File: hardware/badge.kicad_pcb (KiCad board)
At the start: 2 copper layers, 88 x 156.6 mm, 125 parts, among them J1 Micro_SD_Card, J2 MY-18650-01, J3 Conn_01x40, J4 USB_C_Receptacle_USB2.0_14P, J5 MY-18650-01, Q1 AO3400A, Q3 AO3400A, SW1 SW_Push, SW10 SW_Push, SW11 SW_Push, SW12 SW_Push, SW13 SW_Push, SW14 SW_Push, SW15 SW_Push, SW16 SW_Push, SW17 SW_Push, SW18 SW_Push, SW19 SW_Push, SW2 SW_Push, SW20 SW_Push, SW21 SW_Push, SW22 SW_Push, SW23 SW_Push, SW25 SW_Push, SW26 SW_Push, SW27 SW_Push, SW28 SW_Push, SW29 SW_Push, SW3 SW_Push, SW30 SW_Push, SW31 SW_Push, SW33 SW_Push, SW34 SW_Push, SW35 SW_Push, SW36 SW_Push, SW37 SW_Push, SW38 SW_Push, SW39 SW_Push, SW4 SW_Push, SW5 SW_Push, SW57 MK-12C02-G020, SW58 SKRHABE010, SW6 SW_Push, SW7 SW_Push, SW8 BOOT, SW9 SW_Push, U1 ESP32-S3-WROOM-1, U10 PCA9555PW, U11 PCA9555PW, U3 BQ24075RGT, U4 TLV62569DBV, U5 BME280, U6 USBLC6-2P6, U7 BMI270, U8 Ai-Thinker-Ra-02, U9 MAX98357A

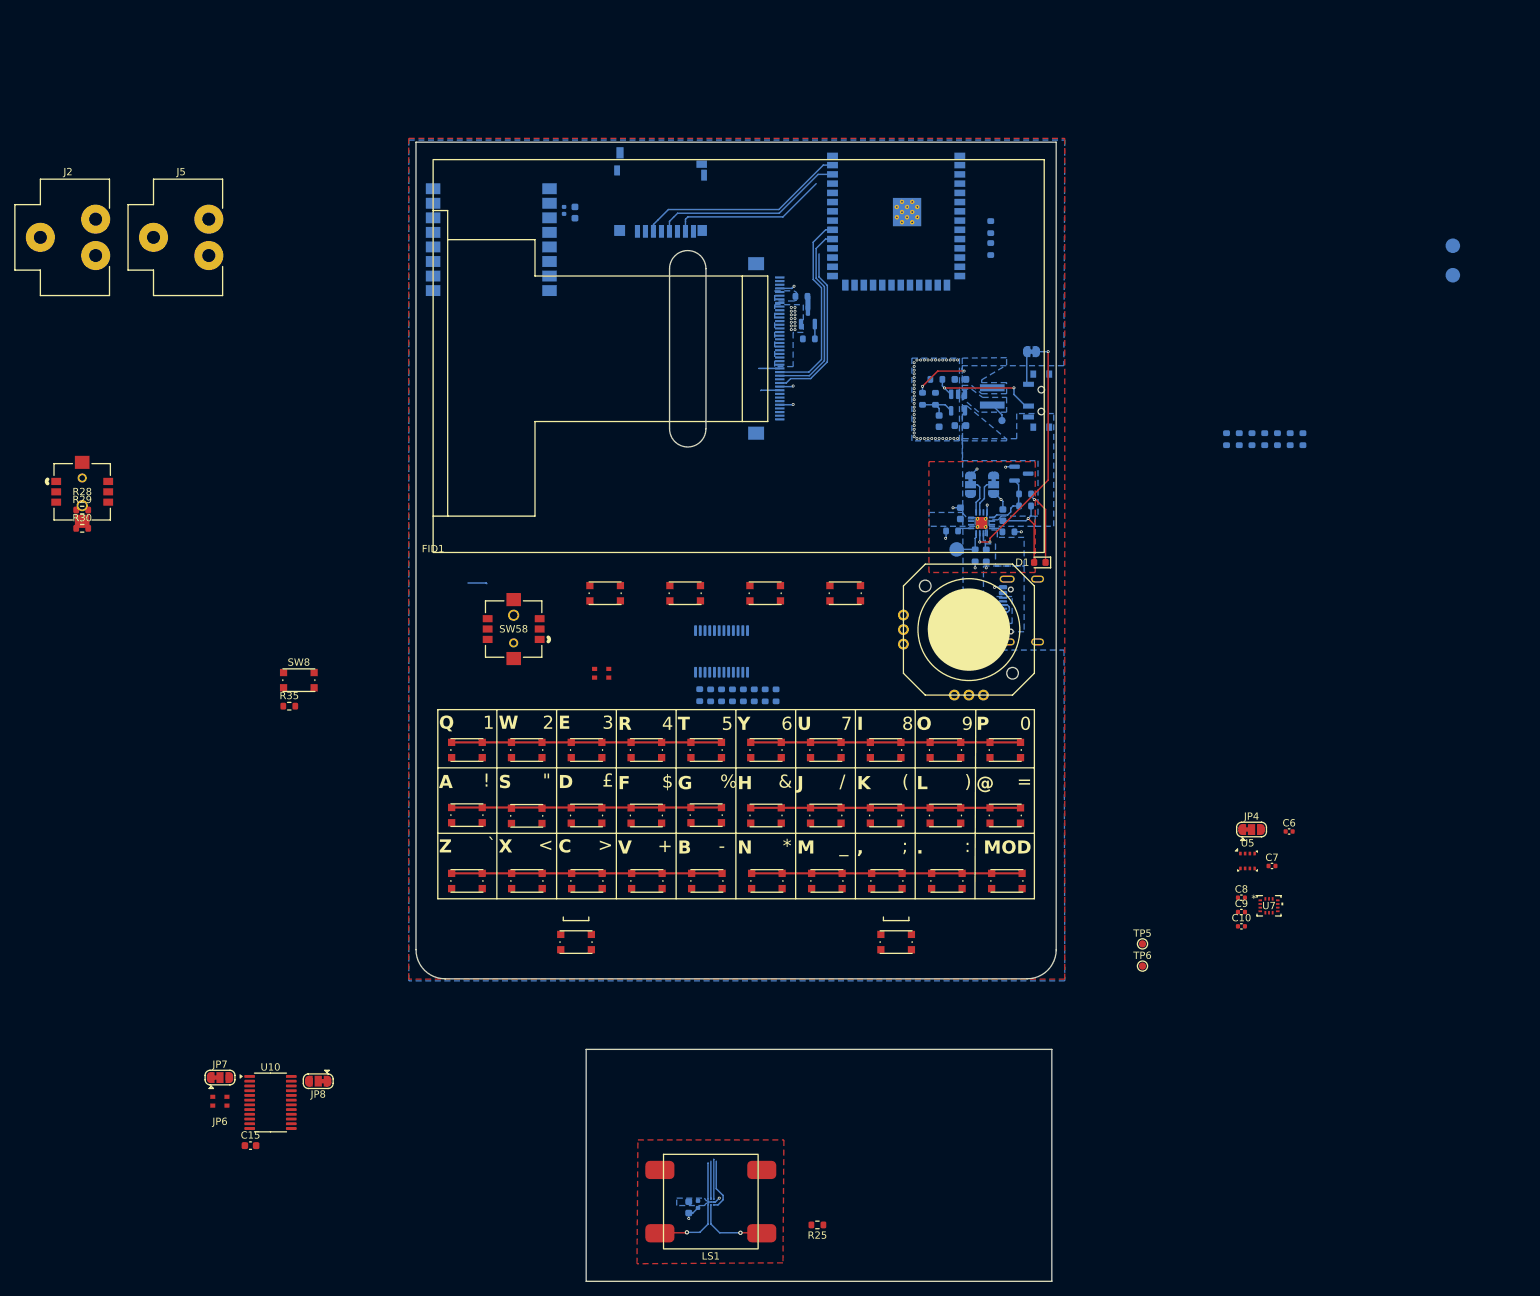
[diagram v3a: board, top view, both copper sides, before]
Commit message: Move battery on top
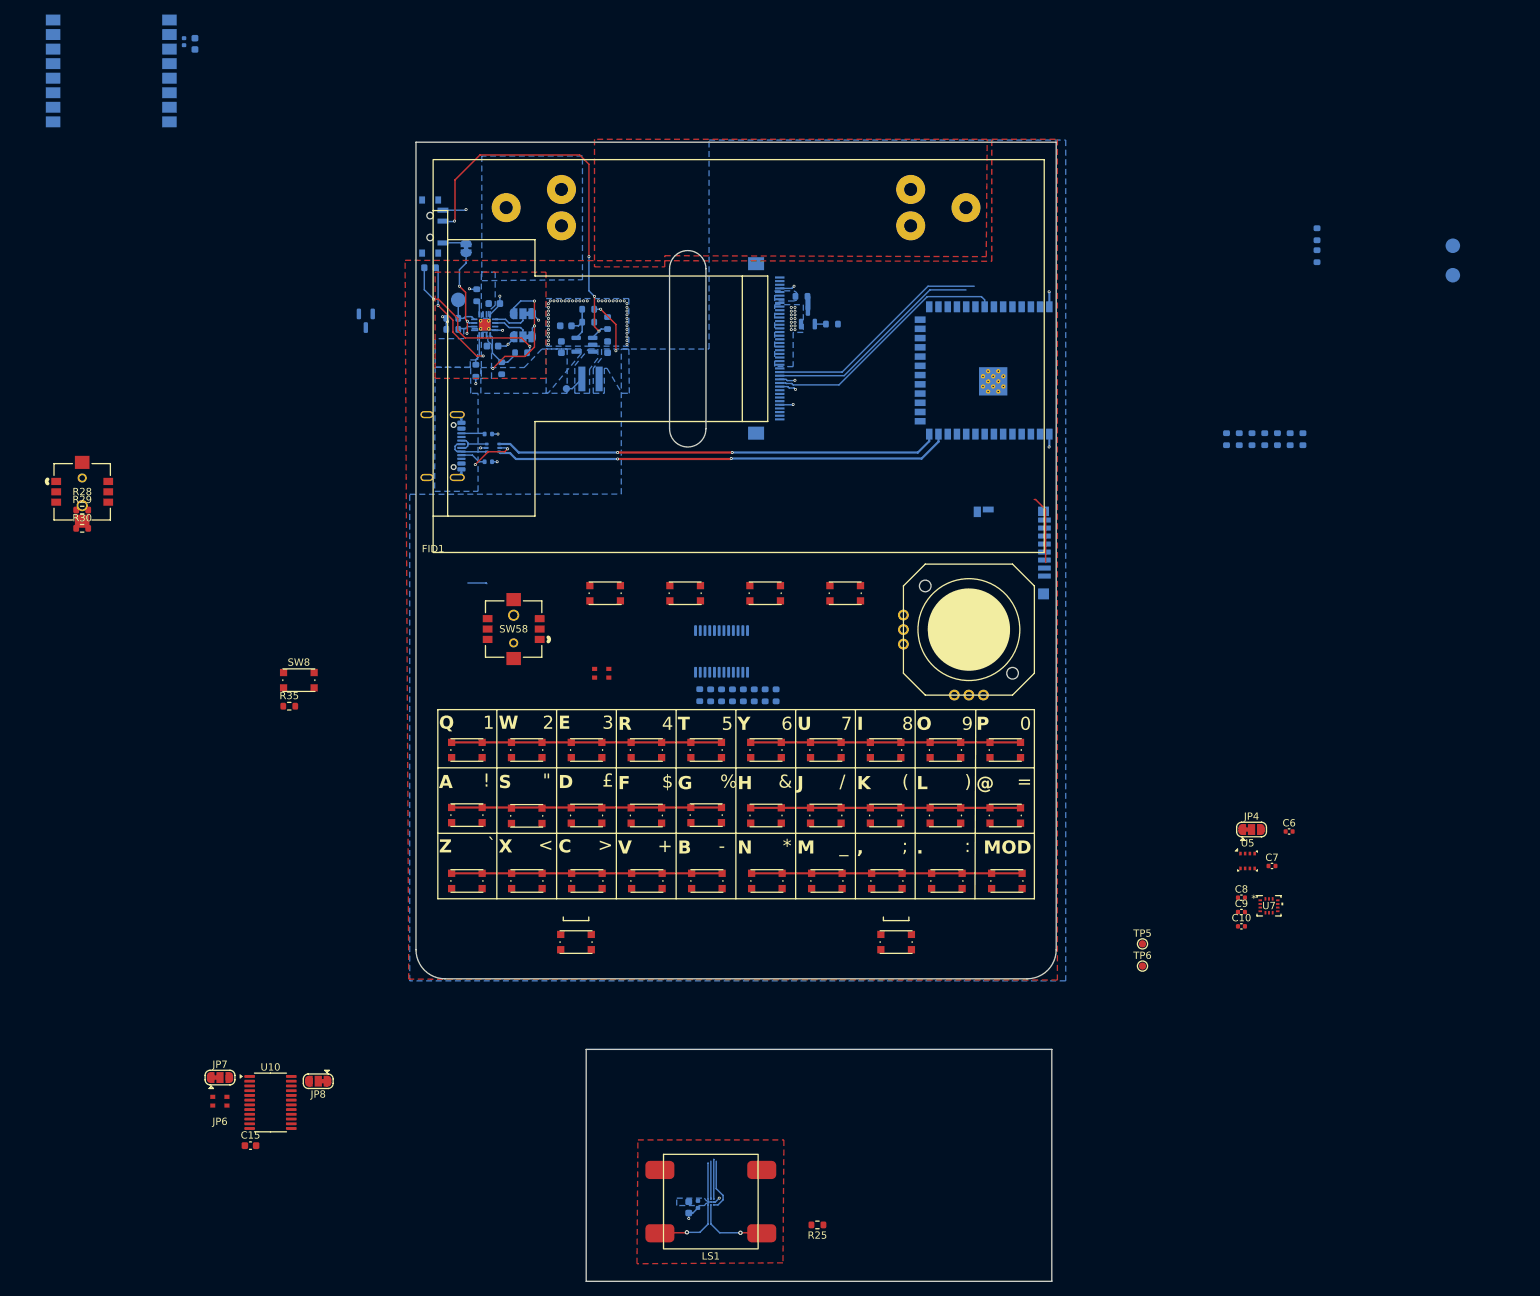
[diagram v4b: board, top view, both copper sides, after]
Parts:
- D1, J2, J5: moved to B.Cu
- moved J2 119.7 mm to (152.8, 40.0), turned to 180 degrees
- moved D1 93.1 mm to (82.9, 48.3), turned to 0 degrees
- moved Q1 92.5 mm to (74.1, 55.5), turned to -90 degrees
- moved SW57 86.7 mm to (83.3, 42.6), turned to 90 degrees
- moved J4 84.9 mm to (83.6, 72.8), turned to 90 degrees
- moved R16 79.7 mm to (86.0, 56.7), turned to 180 degrees
- moved JP3 79.0 mm to (87.9, 45.6), turned to 90 degrees
- moved R18 78.9 mm to (86.0, 55.2), turned to 180 degrees
- moved TP3 76.6 mm to (86.8, 52.7), turned to -90 degrees
- moved R17 76.5 mm to (89.2, 62.4), turned to -90 degrees
- moved R24 74.4 mm to (92.8, 62.1), turned to -90 degrees
- moved C5 73.9 mm to (91.5, 59.0), turned to 0 degrees
- moved U3 73.5 mm to (90.5, 56.1), turned to -90 degrees
- moved R20 72.9 mm to (89.3, 52.0), turned to 90 degrees
- moved R23 71.9 mm to (95.4, 59.9)
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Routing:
- net /mcu/USB_D-: track 0.00 -> 62.8 mm, vias 0 -> 2
- net /mcu/USB_D+: track 0.00 -> 61.2 mm, vias 0 -> 2
- net Net-(SW57-B): track 15.7 -> 53.8 mm, vias 2 -> 4
- net /mcu/SD_CMD: track 28.9 -> 0.00 mm
- net /mcu/SD_CLK: track 26.5 -> 0.00 mm
- net VSYS: track 11.9 -> 37.5 mm, vias 1 -> 6
- net Net-(D1-K): track 10.3 -> 32.2 mm, vias 1 -> 2
- net /mcu/SD_D0: track 21.7 -> 0.00 mm
- net VUSB: track 33.7 -> 19.4 mm, vias 3 -> 5
- net /lcd/SPI_CLK: track 23.1 -> 34.4 mm
- net GND: track 27.3 -> 36.1 mm, vias 77 -> 76
- net /lcd/SPI_MISO: track 26.4 -> 31.6 mm
- net /lcd/SPI_MOSI: track 25.7 -> 30.5 mm
- net /lcd/RESET: track 2.86 -> 0.00 mm
- net Net-(U3-ILIM): track 1.62 -> 4.26 mm
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
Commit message: Create a preliminary routing
Disconnect the LORA module from the lcd bus
Add netclass and lenght matching rule for the LCD signals
Use Bus for spi syglas for easy netclass association
Remove cutaway jumper for the io expansions, and hardcode the address
Routed the keyboard matrix
Change the LCD resistor to 1202
Fix the0Ohm resistor footprint
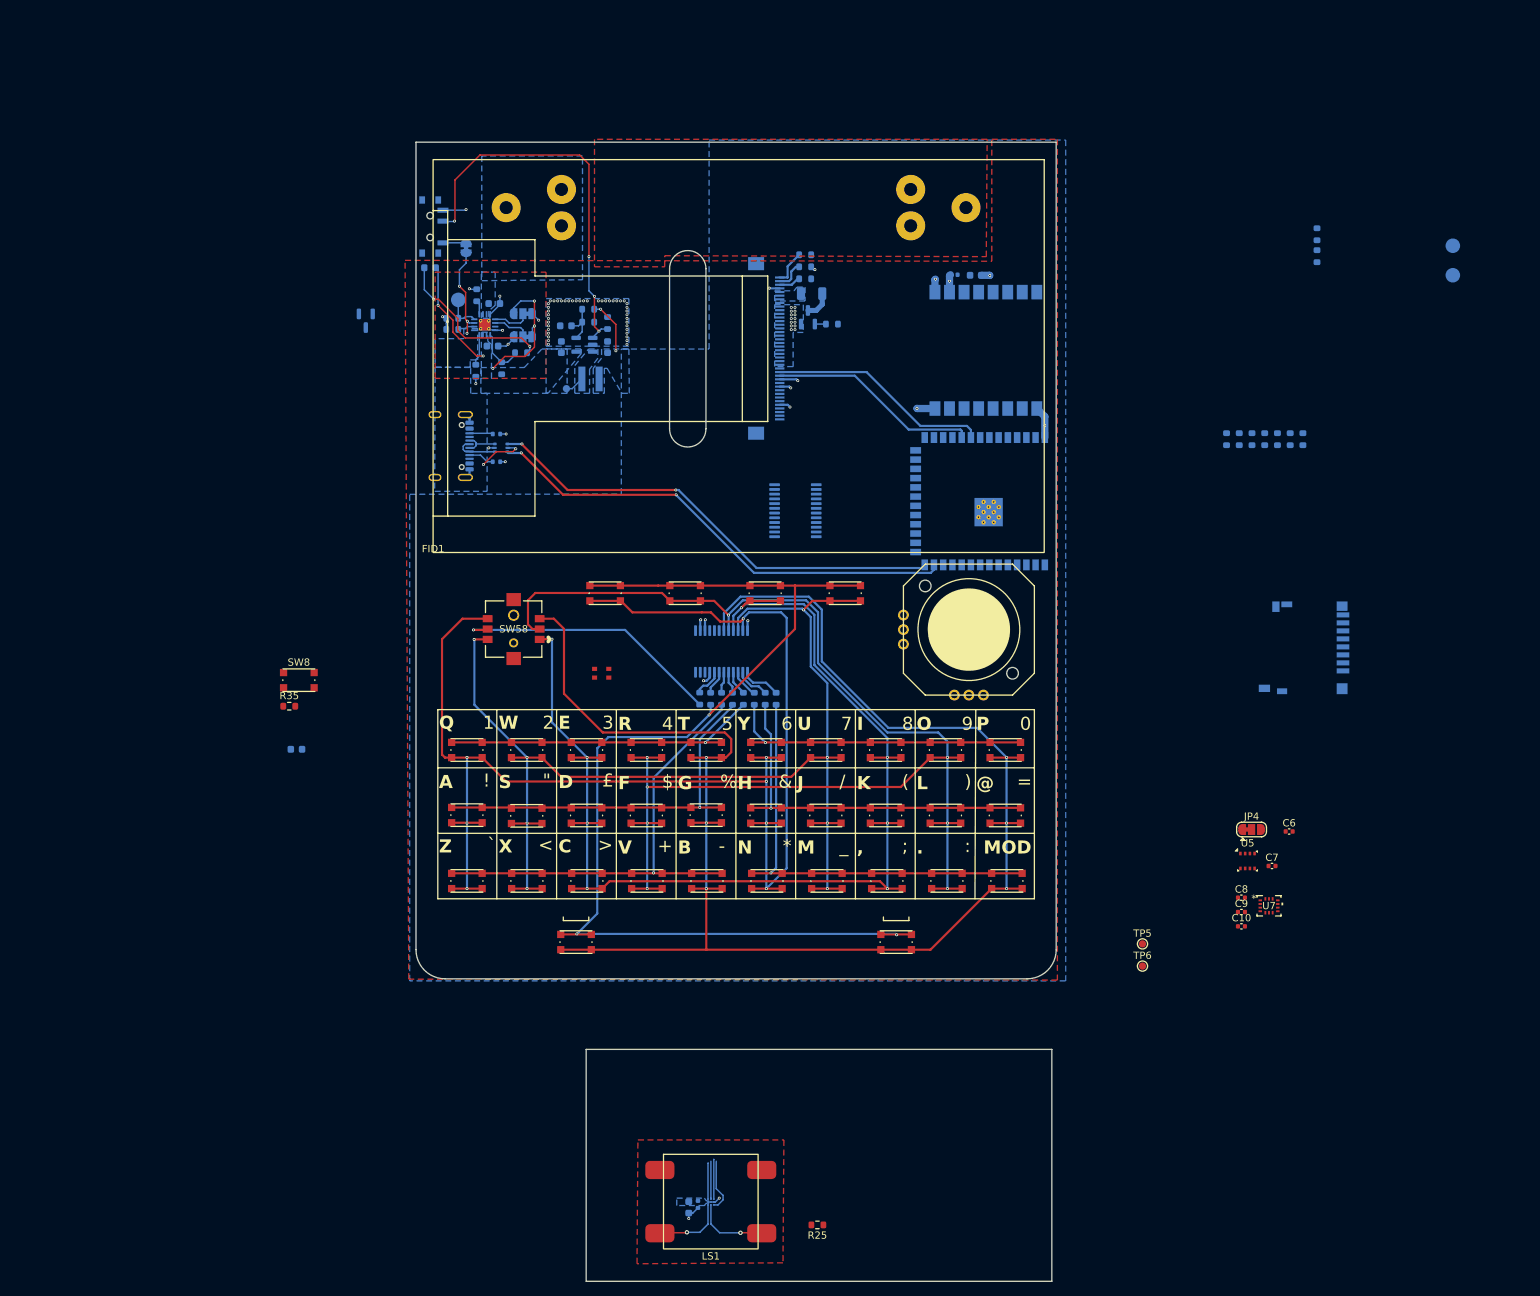
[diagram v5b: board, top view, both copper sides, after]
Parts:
- removed JP6: SolderJumper_3_Bridged12, lib:microfono
- removed JP7, JP8: SolderJumper_3_Bridged12, Jumper:SolderJumper-3_P1.3mm_Bridged12_RoundedPad1.0x1.5mm
- C15, R29, R30, U10: moved to B.Cu
- R28: footprint lib:SKRHABE010_ALPS -> Resistor_SMD:R_0603_1608Metric; moved to B.Cu
- R32: footprint Resistor_SMD:R_0603_1608Metric -> Resistor_SMD:R_1206_3216Metric
- moved U8 126.2 mm to (159.3, 59.6), turned to -90 degrees
- moved C12 111.9 mm to (157.9, 49.3), turned to 0 degrees
- moved C11 110.6 mm to (155.0, 49.2), turned to 180 degrees
- moved U10 108.7 mm to (133.2, 81.7), turned to 180 degrees
- moved R30 106.2 mm to (134.5, 46.5), turned to 180 degrees
- moved R29 104.8 mm to (134.5, 48.1), turned to 180 degrees
- moved R28 103.6 mm to (134.5, 49.8)
- moved C15 54.8 mm to (64.6, 114.5), turned to 180 degrees
- moved J1 43.1 mm to (203.1, 100.5)
- moved U1 18.0 mm to (162.2, 80.4)
- moved R32 1.45 mm to (135.4, 51.8)
- moved J4 1.12 mm to (84.7, 72.8)
- moved R26 1.12 mm to (92.1, 74.9)
- moved R27 1.12 mm to (92.1, 71.1)
- moved U6 1.12 mm to (92.7, 73.0)
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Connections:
- net /lcd/SPI_CS renamed /LCD.CS
- J3 pad 11: /lcd/SPI_CLK -> /LCD.CLK
- J3 pad 13: /lcd/SPI_MOSI -> /LCD.MOSI
- J3 pad 14: /lcd/SPI_MISO -> /LCD.MISO
- U1 pad 31: /lcd/SPI_MOSI -> /LCD.MOSI
- U1 pad 32: /lcd/SPI_MISO -> /LCD.MISO
- U1 pad 33: /lcd/SPI_CLK -> /LCD.CLK
- U10 pad 2: Net-(JP7-C) -> GND
- U10 pad 21: Net-(JP8-C) -> +3.3V
- U10 pad 3: Net-(JP6-C) -> GND
- U8 pad 12: /lcd/SPI_CLK -> unconnected-(U8-SCK-Pad12)
- U8 pad 13: /lcd/SPI_MISO -> unconnected-(U8-MISO-Pad13)
- U8 pad 14: /lcd/SPI_MOSI -> unconnected-(U8-MOSI-Pad14)
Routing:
- net Net-(U11-IO0_3): track 0.00 -> 229.7 mm, vias 0 -> 6
- net Net-(U11-IO0_7): track 0.00 -> 195.6 mm, vias 0 -> 8
- net Net-(U11-IO0_4): track 0.00 -> 183.7 mm, vias 0 -> 8
- net Net-(U11-IO0_5): track 0.00 -> 165.2 mm, vias 0 -> 8
- net Net-(U11-IO0_6): track 0.00 -> 162.8 mm, vias 0 -> 8
- net Net-(R14-Pad2): track 0.00 -> 157.7 mm, vias 0 -> 3
- net Net-(R15-Pad2): track 0.00 -> 37.3 mm, vias 0 -> 1
- net /lcd/SPI_CLK: track 34.4 -> 0.00 mm
- net /lcd/SPI_MISO: track 31.6 -> 0.00 mm
- net /LCD.MISO: track 0.00 -> 30.6 mm
- net /lcd/SPI_MOSI: track 30.5 -> 0.00 mm
- net /LCD.MOSI: track 0.00 -> 29.1 mm
- net Net-(R13-Pad2): track 37.2 -> 64.2 mm, vias 0 -> 1
- net Net-(R8-Pad2): track 37.2 -> 60.6 mm, vias 0 -> 1
- net Net-(R12-Pad2): track 37.1 -> 53.0 mm, vias 0 -> 1
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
